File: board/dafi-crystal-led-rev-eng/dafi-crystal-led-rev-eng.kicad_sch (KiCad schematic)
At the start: 19 parts, among them SW1 SW_DPST_x2, U1 STM8L051F3P, U2 LIS2DW12

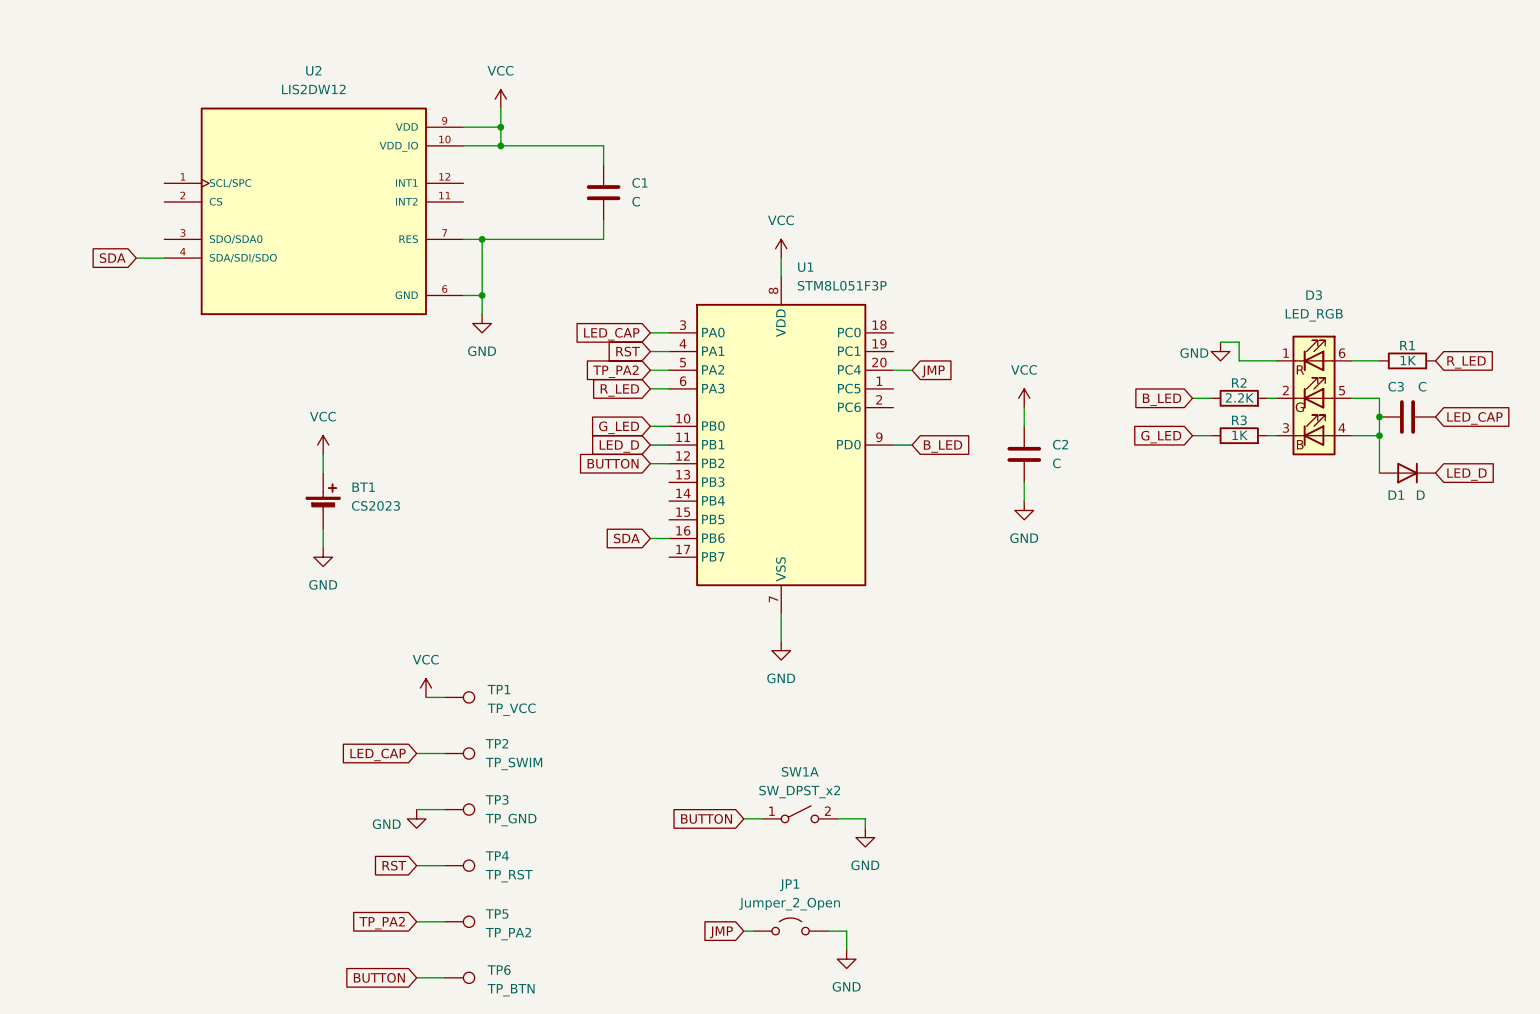
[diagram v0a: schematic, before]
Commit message: updated pins for accelerometer, made .ioc8 config file
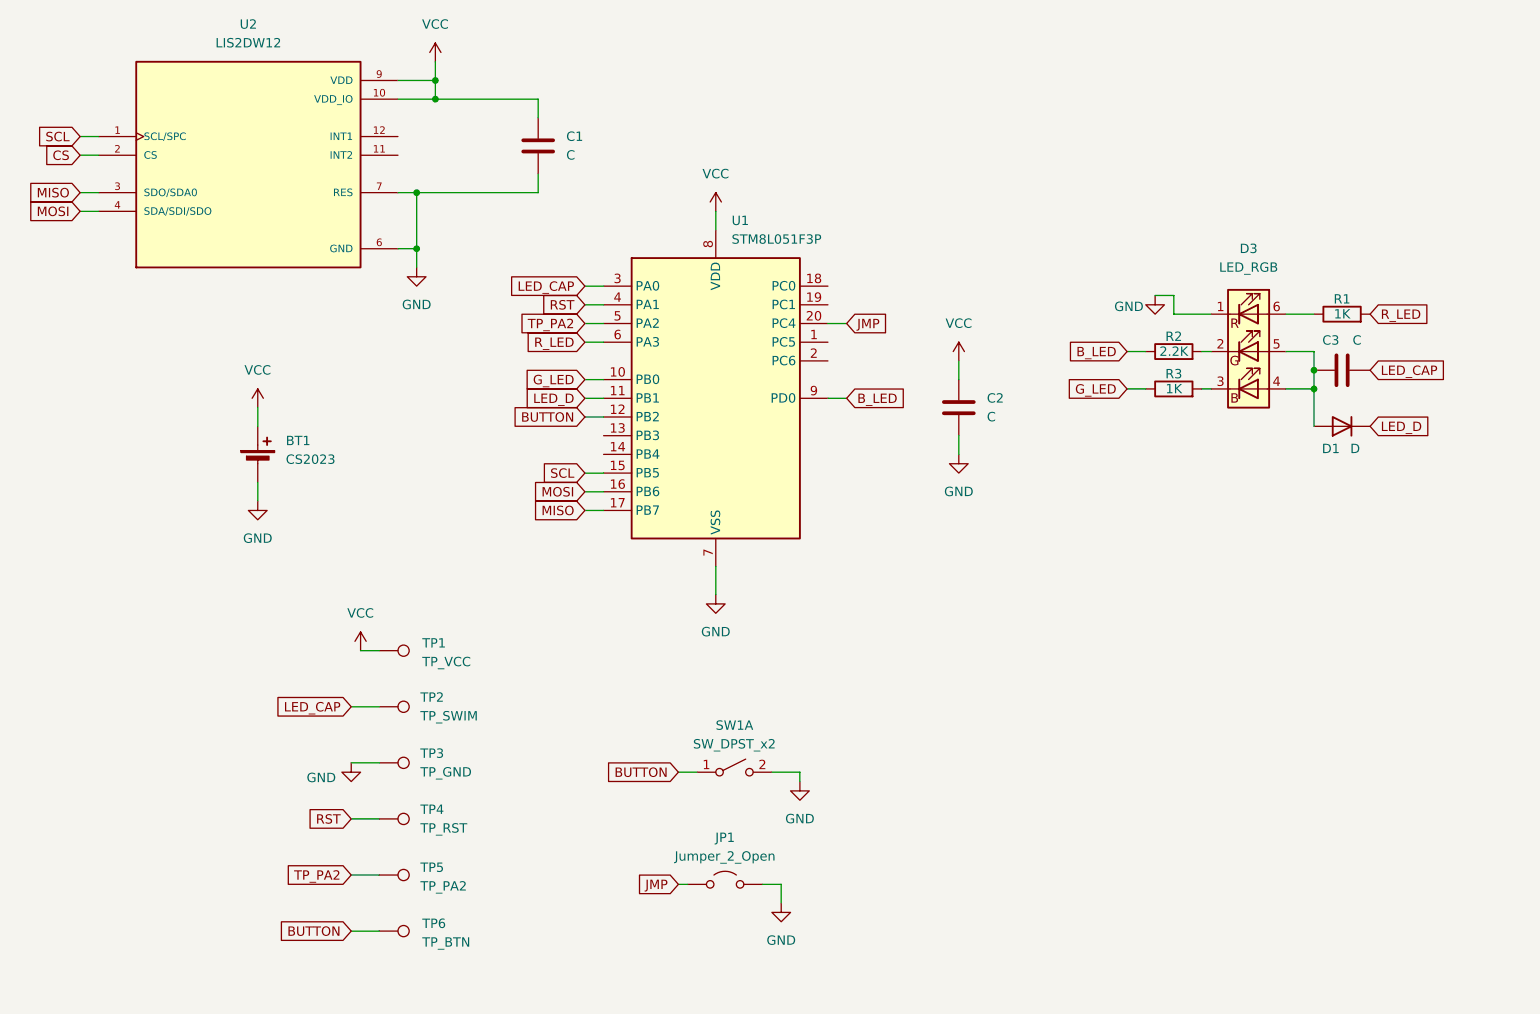
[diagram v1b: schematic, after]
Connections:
- net SCL: now reaches U2.1 (SCL/SPC)
- net SCL: now also U1.15 (PB5)
- net CS: now reaches U2.2 (CS)
- net MISO: now reaches U2.3 (SDO/SDA0)
- net MISO: now also U1.17 (PB7)
- net SDA renamed MOSI
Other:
- moved on the sheet: BT1, C1, C2, C3, D1, D3, JP1, R1, R2, R3, SW1A, TP1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

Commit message: messing around with uart
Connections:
- net CS: now also U1.14 (PB4)
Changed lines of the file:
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@@
+	(wire
+		(pts
+			(xy 123.19 105.41) (xy 125.73 105.41)
+		)
+		(stroke
+			(width 0)
+			(type default)
+		)
+	)
 	(wire
 		(pts
@@
 			(effects
 				(font
+					(size 1.27 1.27)
+				)
+				(justify right)
+				(hide yes)
+			)
+		)
+	)
+	(global_label "CS"
+		(shape input)
+		(at 123.19 105.41 180)
+		(fields_autoplaced yes)
+		(effects
+			(font
+				(size 1.27 1.27)
+			)
+			(justify right)
+		)
+		(property "Intersheetrefs" "${INTERSHEET_REFS}"
+			(at 117.7253 105.41 0)
+			(effects
+				(font
